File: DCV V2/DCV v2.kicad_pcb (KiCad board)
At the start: 2 copper layers, 97.7 x 59.7 mm, 46 parts, among them J1 ANT, J10 TP3, J2 TP6, J3 LO, J4 PWR, J5 Audio, J6 TP1, J7 TP2, J8 TP5, J9 TP4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

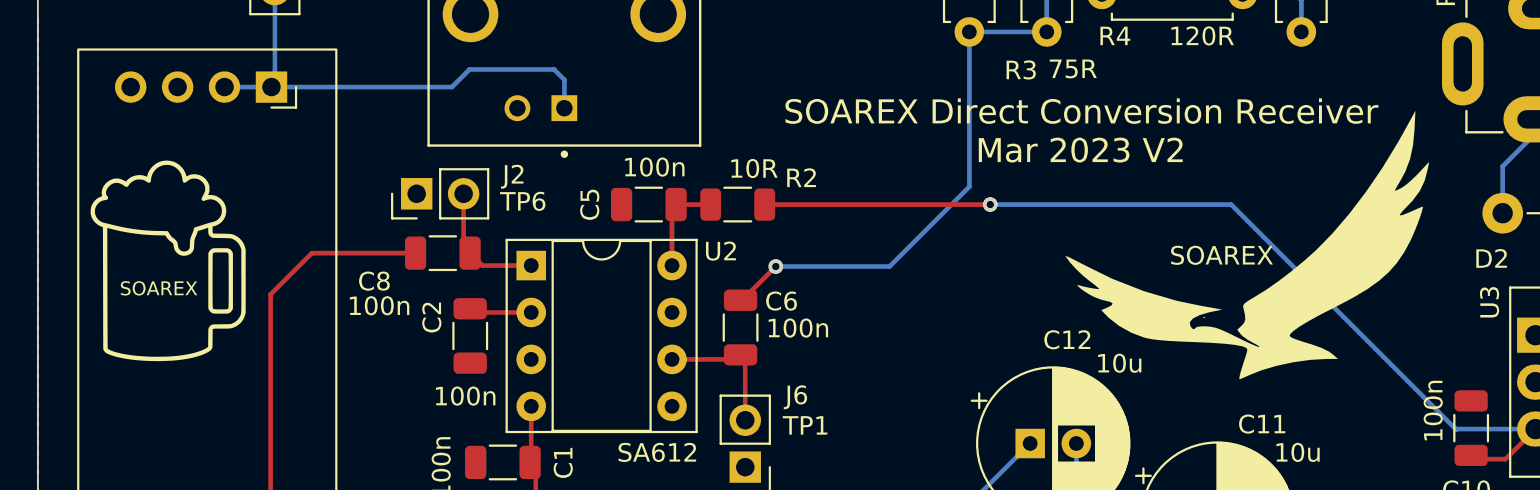
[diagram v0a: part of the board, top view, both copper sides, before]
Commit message: Added SOAREX Logo
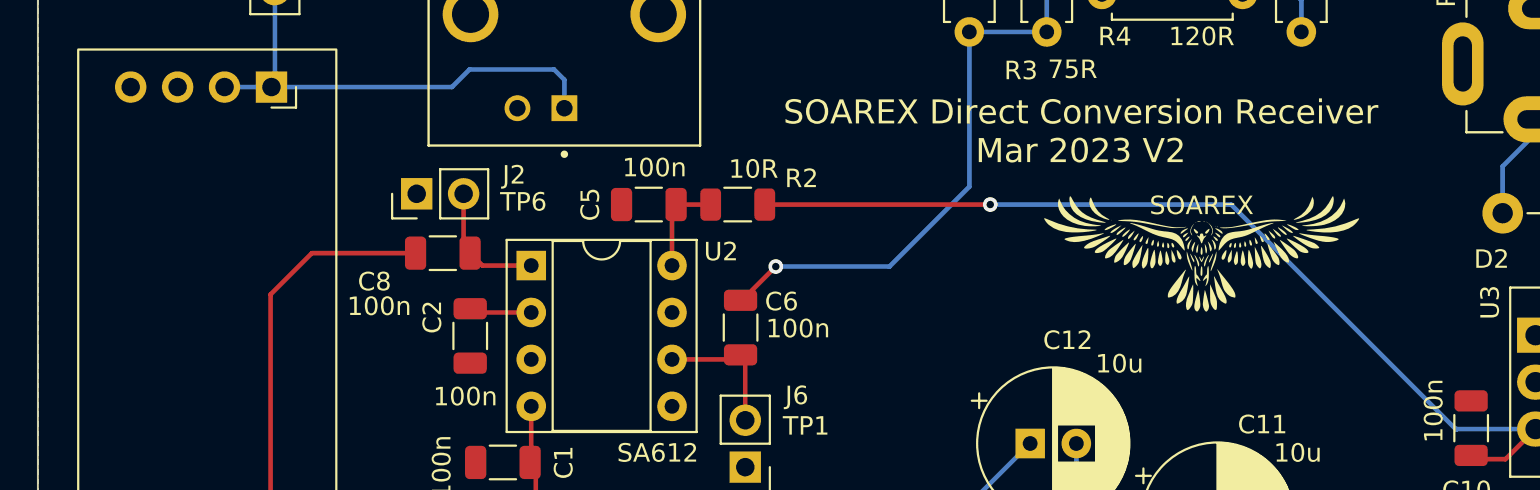
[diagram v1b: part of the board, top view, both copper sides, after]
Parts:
- removed the G*** at (87.3, 49.5)
- removed REF**: Homebrew_mug, Custom_Images:Homebrew_mug_SOAREX_small
- added G***: LOGO, Custom_Images:SOAREX_Falcon_20mm, F.Cu at (84.7, 44.3)
